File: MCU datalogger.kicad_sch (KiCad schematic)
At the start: 25 parts

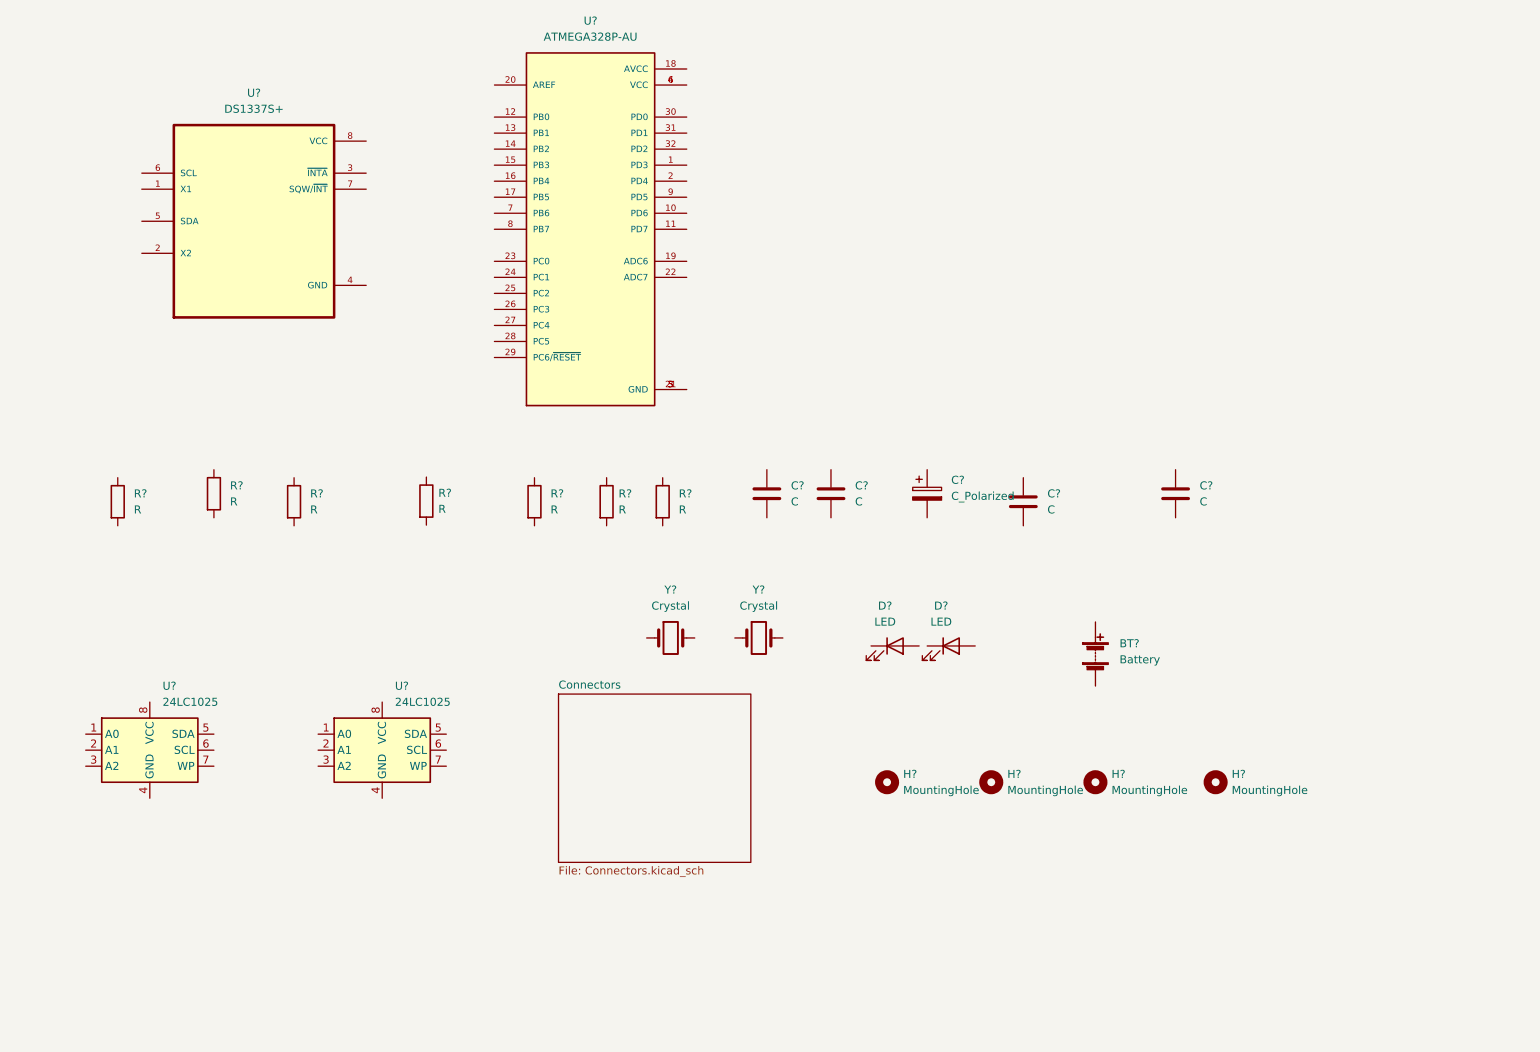
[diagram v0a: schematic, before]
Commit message: changed locations of symbols
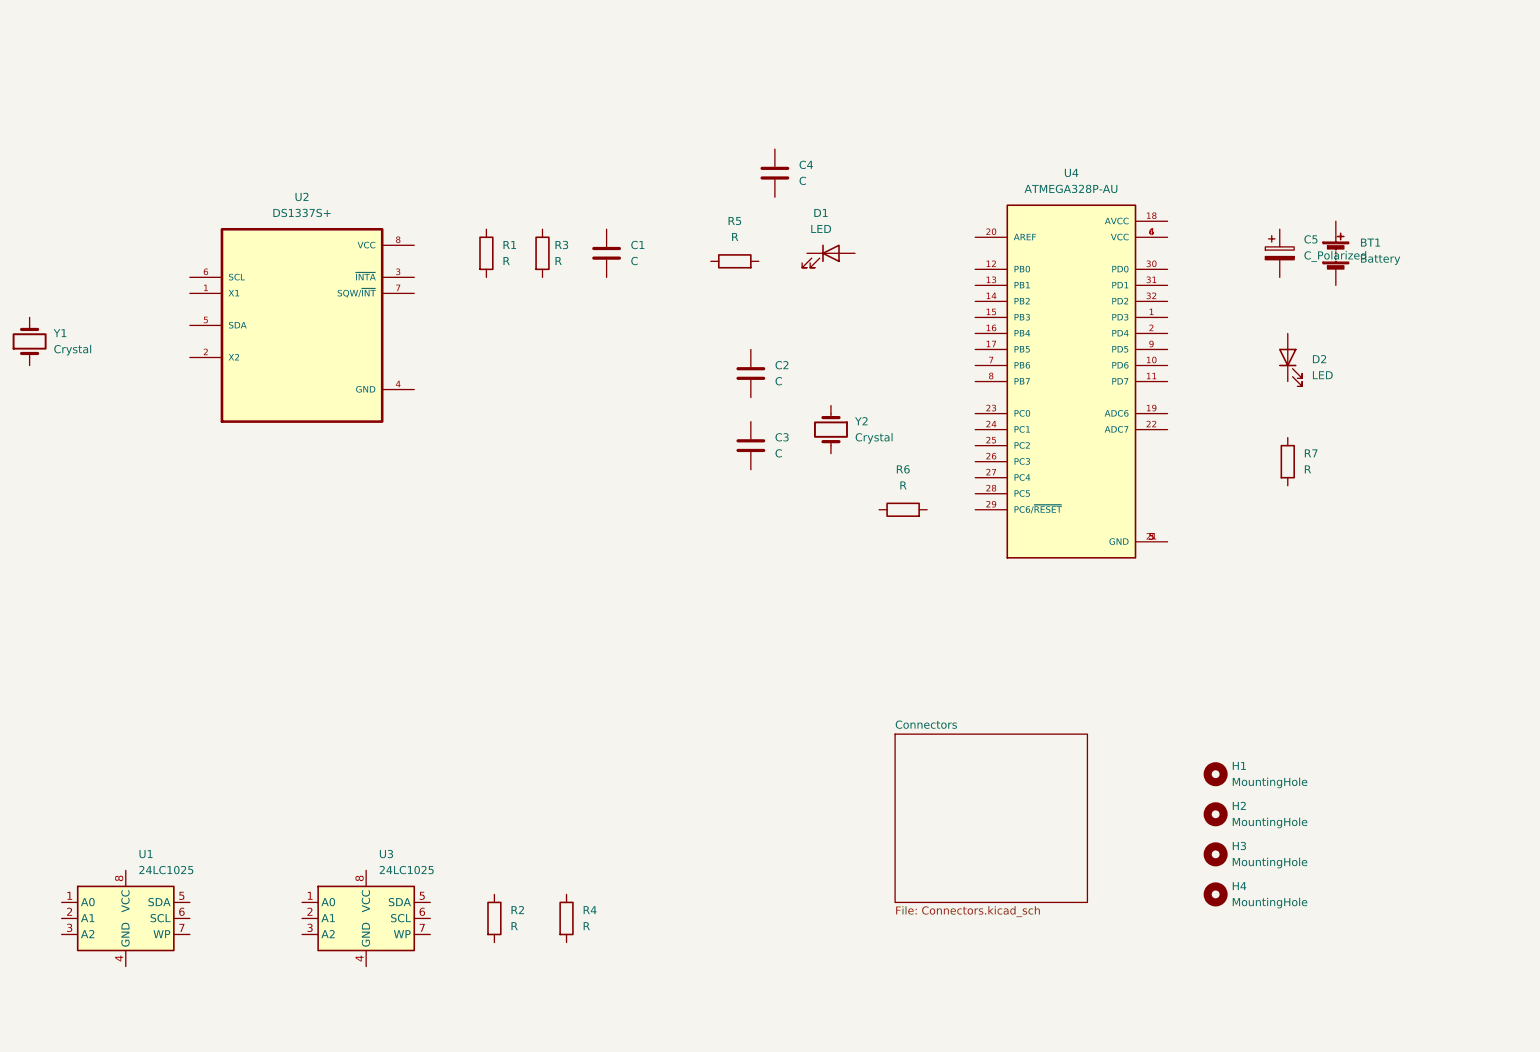
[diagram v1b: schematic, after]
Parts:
- gave numbers to parts that had none: 25
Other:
- moved on the sheet: BT1, C1, C2, C3, C4, C5, D1, D2, H1, H2, H3, H4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

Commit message: Added component values
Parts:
- C1, C4: value C -> 0.1uF
- C2, C3: value C -> 22pF
- C5: value C_Polarized -> 100nF
- R1, R3, R6: value R -> 10K
- R2, R4: value R -> 4.7K
- R5, R7: value R -> 330
- Y1: value Crystal -> 32.768 KHz
- Y2: value Crystal -> 16MHz
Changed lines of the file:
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@@
       (effects (font (size 1.27 1.27)) (justify left))
     )
-    (property "Value" "R" (id 1) (at 245.11 92.7099 0)
+    (property "Value" "330" (id 1) (at 245.11 92.7099 0)
       (effects (font (size 1.27 1.27)) (justify left))
     )
@@
       (effects (font (size 1.27 1.27)) (justify left))
     )
-    (property "Value" "R" (id 1) (at 126.3509 59.6899 0)
+    (property "Value" "10K" (id 1) (at 126.3509 59.6899 0)
       (effects (font (size 1.27 1.27)) (justify left))
     )
@@
       (effects (font (size 1.27 1.27)) (justify left))
     )
-    (property "Value" "C_Polarized" (id 1) (at 245.11 58.8009 0)
+    (property "Value" "100nF" (id 1) (at 245.11 58.8009 0)
       (effects (font (size 1.27 1.27)) (justify left))
     )
@@
     (in_bom yes) (on_board yes) (fields_autoplaced)
     (property "Reference" "R6" (id 0) (at 181.61 92.71 90))
-    (property "Value" "R" (id 1) (at 181.61 95.25 90))
+    (property "Value" "10K" (id 1) (at 181.61 95.25 90))
     (property "Footprint" "" (id 2) (at 181.61 100.838 90)
       (effects (font (size 1.27 1.27)) hide)
@@
       (effects (font (size 1.27 1.27)) (justify left))
     )
-    (property "Value" "R" (id 1) (at 130.81 165.0999 0)
+    (property "Value" "4.7K" (id 1) (at 130.81 165.0999 0)
       (effects (font (size 1.27 1.27)) (justify left))
     )
@@
       (effects (font (size 1.27 1.27)) (justify left))
     )
-    (property "Value" "C" (id 1) (at 138.43 59.6899 0)
+    (property "Value" "0.1uF" (id 1) (at 138.43 59.6899 0)
       (effects (font (size 1.27 1.27)) (justify left))
     )
@@
       (effects (font (size 1.27 1.27)) (justify left))
     )
-    (property "Value" "C" (id 1) (at 161.29 78.7399 0)
+    (property "Value" "22pF" (id 1) (at 161.29 78.7399 0)
       (effects (font (size 1.27 1.27)) (justify left))
     )
@@
       (effects (font (size 1.27 1.27)) (justify left))
     )
-    (property "Value" "R" (id 1) (at 119.38 165.0999 0)
+    (property "Value" "4.7K" (id 1) (at 119.38 165.0999 0)
       (effects (font (size 1.27 1.27)) (justify left))
     )
@@
       (effects (font (size 1.27 1.27)) (justify left))
     )
-    (property "Value" "C" (id 1) (at 161.29 90.1699 0)
+    (property "Value" "22pF" (id 1) (at 161.29 90.1699 0)
       (effects (font (size 1.27 1.27)) (justify left))
     )
@@
       (effects (font (size 1.27 1.27)) (justify right))
     )
-    (property "Value" "Crystal" (id 1) (at 46.99 73.6599 90)
+    (property "Value" "32.768 KHz" (id 1) (at 46.99 73.6599 90)
       (effects (font (size 1.27 1.27)) (justify right))
     )
@@
     (in_bom yes) (on_board yes) (fields_autoplaced)
     (property "Reference" "R5" (id 0) (at 154.94 53.34 90))
-    (property "Value" "R" (id 1) (at 154.94 55.88 90))
+    (property "Value" "330" (id 1) (at 154.94 55.88 90))
     (property "Footprint" "" (id 2) (at 154.94 61.468 90)
       (effects (font (size 1.27 1.27)) hide)
@@
       (effects (font (size 1.27 1.27)) (justify left))
     )
-    (property "Value" "R" (id 1) (at 118.11 59.6899 0)
+    (property "Value" "10K" (id 1) (at 118.11 59.6899 0)
       (effects (font (size 1.27 1.27)) (justify left))
     )
@@
       (effects (font (size 1.27 1.27)) (justify left))
     )
-    (property "Value" "C" (id 1) (at 165.1 46.9899 0)
+    (property "Value" "0.1uF" (id 1) (at 165.1 46.9899 0)
       (effects (font (size 1.27 1.27)) (justify left))
     )
@@
       (effects (font (size 1.27 1.27)) (justify left))
     )
-    (property "Value" "Crystal" (id 1) (at 173.99 87.6299 90)
+    (property "Value" "16MHz" (id 1) (at 173.99 87.6299 90)
       (effects (font (size 1.27 1.27)) (justify left))
     )
@@
     )
     (path "/7dcd83a1-2805-4ad3-978f-e544b7851988"
-      (reference "C1") (unit 1) (value "C") (footprint "")
+      (reference "C1") (unit 1) (value "0.1uF") (footprint "")
     )
     (path "/95c0a31b-7f46-4519-9cf2-f2fd73a4d0c0"
-      (reference "C2") (unit 1) (value "C") (footprint "")
+      (reference "C2") (unit 1) (value "22pF") (footprint "")
     )
     (path "/ae416188-70f7-41c6-a3ed-aaafcf71ac04"
-      (reference "C3") (unit 1) (value "C") (footprint "")
+      (reference "C3") (unit 1) (value "22pF") (footprint "")
     )
     (path "/e27b1c1e-4334-41de-b195-7cb6f531aaad"
-      (reference "C4") (unit 1) (value "C") (footprint "")
+      (reference "C4") (unit 1) (value "0.1uF") (footprint "")
     )
     (path "/4bf2cd36-a049-4742-b6f0-905af5c736ed"
-      (reference "C5") (unit 1) (value "C_Polarized") (footprint "")
+      (reference "C5") (unit 1) (value "100nF") (footprint "")
     )
     (path "/80609c0c-2452-440b-a294-83998571cdad"
@@
     )
     (path "/cbfcdd58-26c9-44ab-8451-779d12b7522f"
-      (reference "R1") (unit 1) (value "R") (footprint "")
+      (reference "R1") (unit 1) (value "10K") (footprint "")
     )
     (path "/9b8f78a2-b3b1-4988-a2fa-cb0275a6b09c"
-      (reference "R2") (unit 1) (value "R") (footprint "")
+      (reference "R2") (unit 1) (value "4.7K") (footprint "")
     )
     (path "/3e60af89-5f8f-4d22-8823-3189b72e486e"
-      (reference "R3") (unit 1) (value "R") (footprint "")
+      (reference "R3") (unit 1) (value "10K") (footprint "")
     )
     (path "/7657c0e2-b07d-42b9-81ed-d40564fcfa90"
-      (reference "R4") (unit 1) (value "R") (footprint "")
+      (reference "R4") (unit 1) (value "4.7K") (footprint "")
     )
     (path "/c7439e90-c6b8-47b2-9d17-a06c395fe26e"
-      (reference "R5") (unit 1) (value "R") (footprint "")
+      (reference "R5") (unit 1) (value "330") (footprint "")
     )
     (path "/5f16c44d-9ecb-40d4-82ed-50d42158e678"
-      (reference "R6") (unit 1) (value "R") (footprint "")
+      (reference "R6") (unit 1) (value "10K") (footprint "")
     )
     (path "/35318176-26bc-4124-8d52-94cac88c25bb"
-      (reference "R7") (unit 1) (value "R") (footprint "")
+      (reference "R7") (unit 1) (value "330") (footprint "")
     )
     (path "/b00f55cd-2fd0-4be3-95f5-ff701f60c355"
@@
     )
     (path "/b02d4c0e-3f8e-40e2-8926-541d5e76e0da"
-      (reference "Y1") (unit 1) (value "Crystal") (footprint "")
+      (reference "Y1") (unit 1) (value "32.768 KHz") (footprint "")
     )
     (path "/eee18d97-07d9-4b11-a553-c0c8b9c9a7c1"
-      (reference "Y2") (unit 1) (value "Crystal") (footprint "")
-    )
-  )
+      (reference "Y2") (unit 1) (value "16MHz") (footprint "")
+    )
+  )

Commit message: Completed symbol to footprint associations
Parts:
- BT1: footprint (none) -> Connector_PinHeader_2.54mm:PinHeader_1x02_P2.54mm_Vertical
- C1, C2, C3, C4, C5: footprint (none) -> Capacitor_SMD:C_0805_2012Metric
- D1, D2: footprint (none) -> LED_SMD:LED_0805_2012Metric
- H1, H2, H3, H4: footprint (none) -> MountingHole:MountingHole_2.1mm
- R1, R2, R3, R4, R5, R6, R7: footprint (none) -> Resistor_SMD:R_0805_2012Metric
- U1, U3: footprint (none) -> Package_SO:SOIC-8_5.23x5.23mm_P1.27mm
- U2: footprint SOIC127P600X175-8N -> footprints:SOIC127P600X175-8N
- U4: footprint QFP80P900X900X120-32N -> footprints:QFP80P900X900X120-32N
- Y1, Y2: footprint (none) -> Crystal:Crystal_SMD_5032-2Pin_5.0x3.2mm_HandSoldering

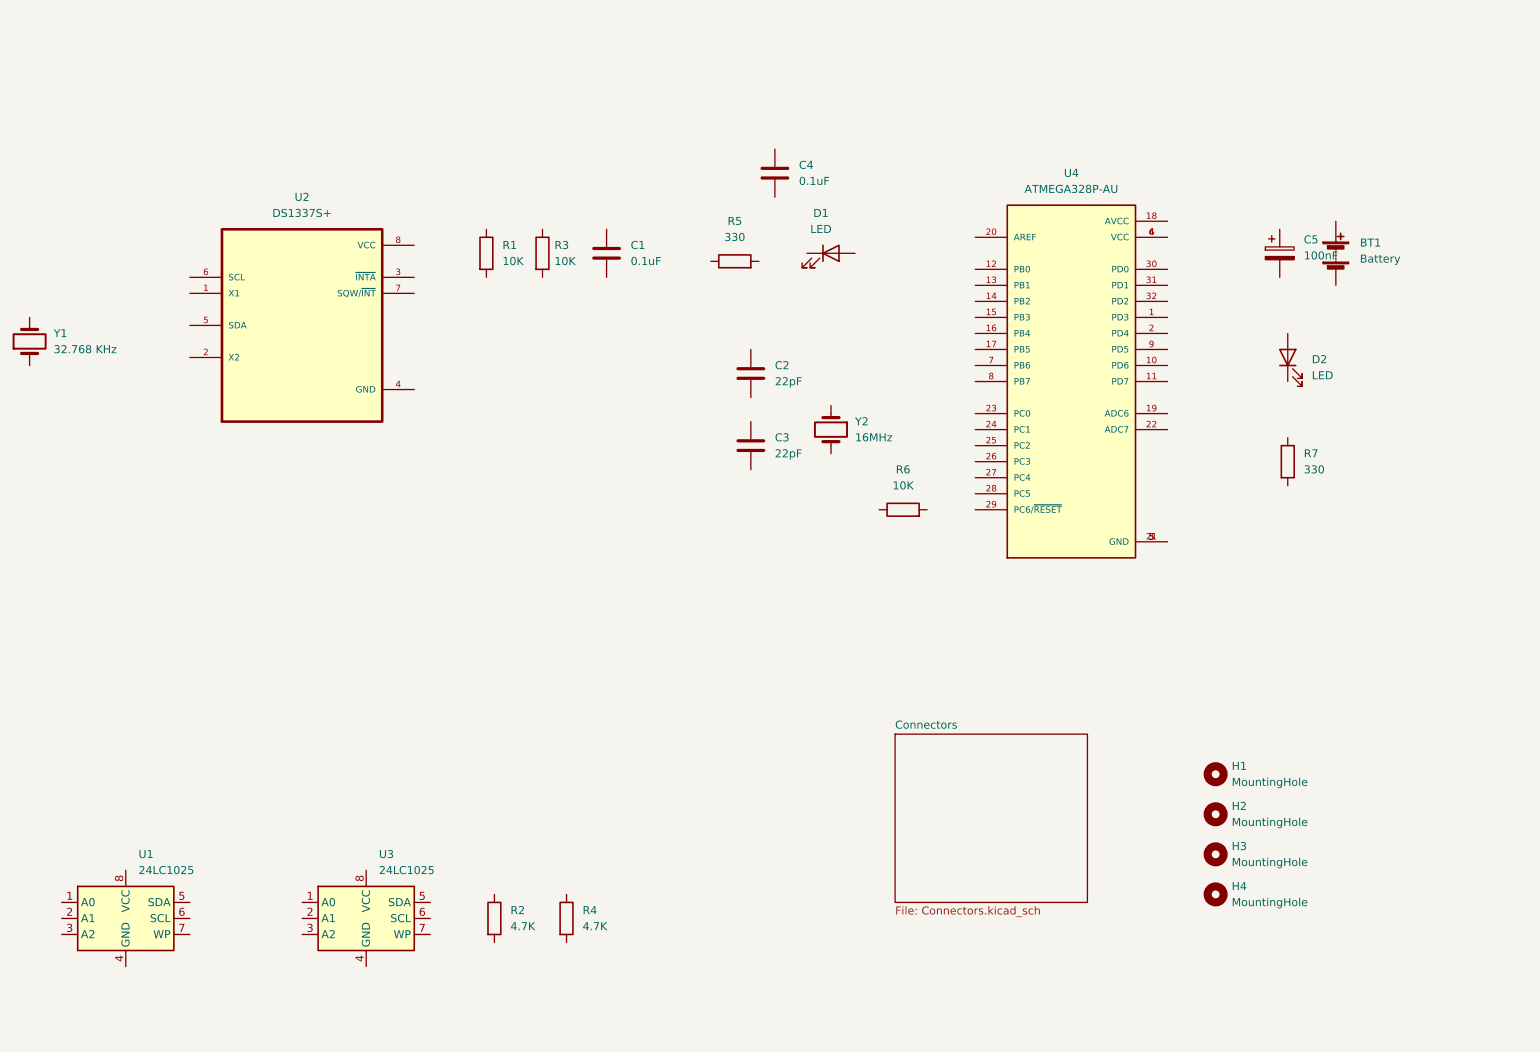
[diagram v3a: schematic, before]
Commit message: Completed wiring of main sheet
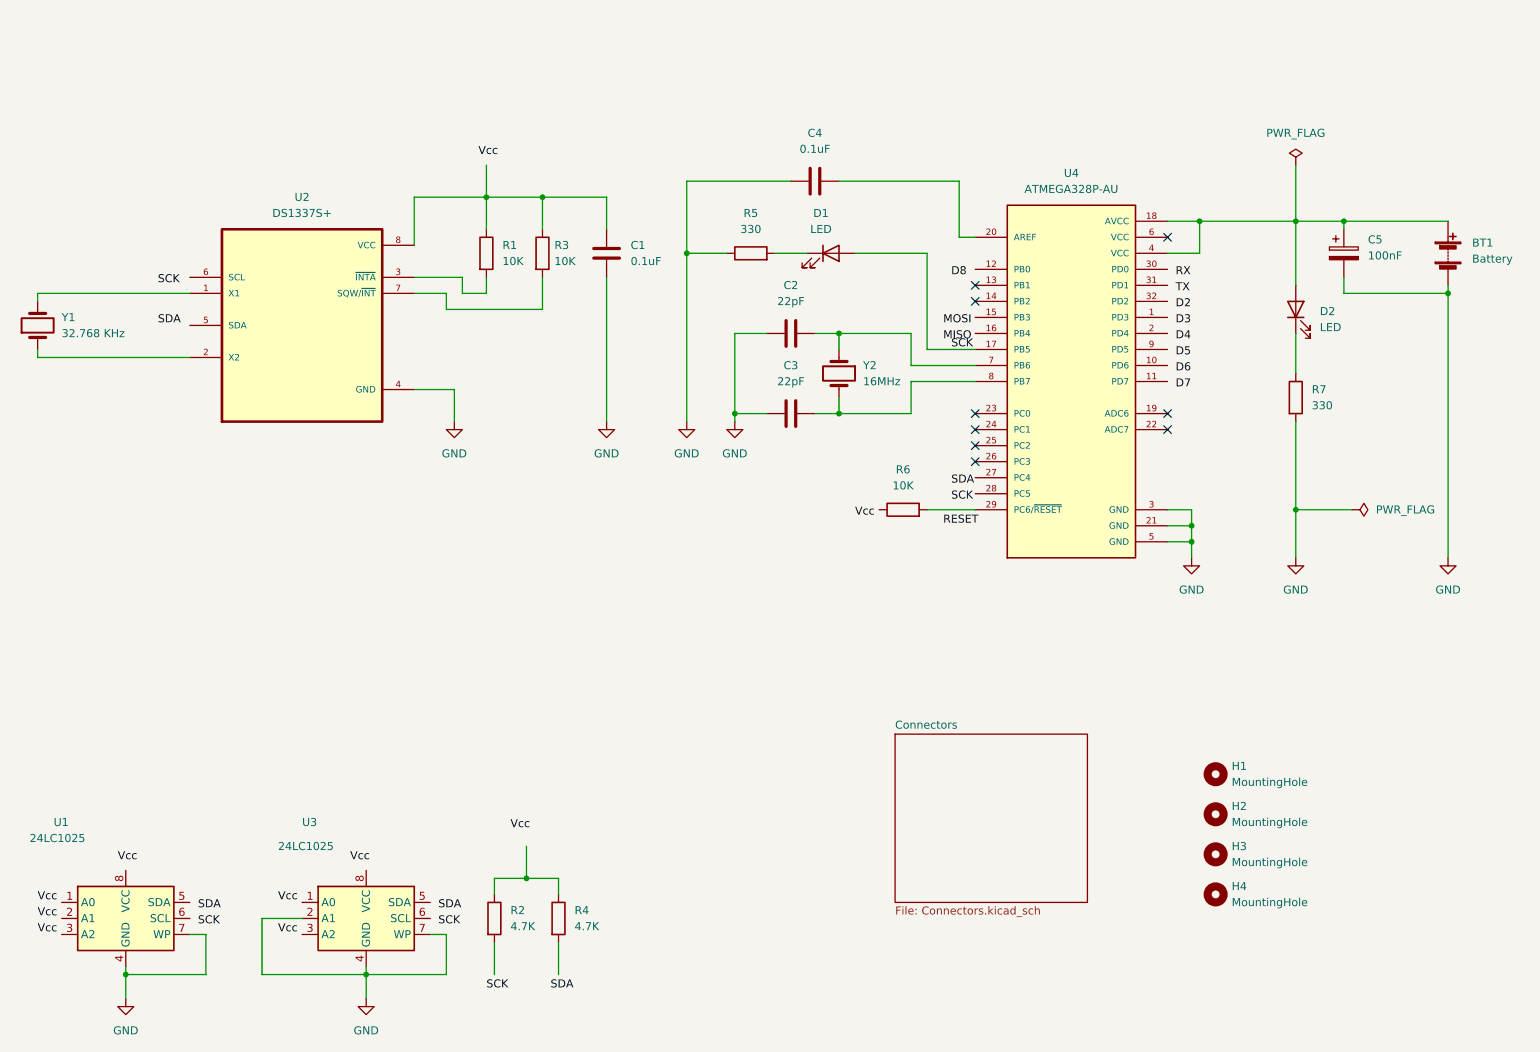
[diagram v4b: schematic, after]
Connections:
- net GND: now reaches U3.2 (A1)
- net GND: now also BT1.2 (-), C1.2, C2.1, C3.1, C4.1, C5.2, R5.1, R7.2, U1.4 (GND), U1.7 (WP), U2.4 (GND), U3.4 (GND), U3.7 (WP), U4.21 (GND), U4.3 (GND), U4.5 (GND)
- net at D2.1 (K): now also R7.1
- net at D2.2 (A): now also BT1.1 (+), C5.1, U4.18 (AVCC), U4.4 (VCC)
- net at R3.1: now also C1.1, R1.1, U2.8 (VCC)
- net at R3.2: now also U2.7 (SQW/~{INT})
- net SCK: now reaches U4.17 (PB5)
- net SCK: now also D1.2 (A)
- net at U4.20 (AREF): now also C4.2
- net at U4.29 (PC6/~{RESET}): now also R6.2
- net at U4.6 (VCC): no longer U4.4 (VCC)
- net at U4.7 (PB6): now also C2.2, Y2.1
- net at U4.8 (PB7): now also C3.2, Y2.2
- net at R4.1: now also R2.1
- net at D1.1 (K): now also R5.2
- net at U2.1 (X1): now also Y1.2
- net at U2.2 (X2): now also Y1.1
- net at U2.3 (~{INTA}): now also R1.2
- no-connect marks 0 -> 9
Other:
- moved on the sheet: BT1, C2, C3, C4, C5, D2, R4, R5, R7, Y1, Y2
